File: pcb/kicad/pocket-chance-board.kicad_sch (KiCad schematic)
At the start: 144 parts, among them J1 SWD, J2 USB4085-GF-A, J3 LiPo JST-PH 2.0mm (1 = + RED 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, J4 LCD 1.54in ST7789 module, JST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, J5 Speaker JST-PH, J6 microSD Molex 104031-0811, J7 STEMMA QT, J8 Expansion (6 = VBAT_SENSE ADC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, J9 LCD header 2.54 mm (wire by n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, Q1 FS8205A, Q3 AO3400A, Q4 AO3401A, Q6 AO3401A (DNP: fit only for a 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, SW1 BOOT, SW10 DPAD LEFT PTS645SM43SMTR92, SW11 DPAD RIGHT PTS645SM43SMTR92, SW12 DPAD PRESS PTS645SM43SMTR92, SW2 RESET, SW3 POWER PCM12, SW4 A PTS125SM43SMTR2LFS, SW5 B PTS125SM43SMTR2LFS, SW6 X PTS125SM43SMTR2LFS, SW7 Y PTS125SM43SMTR2LFS, SW8 DPAD UP PTS645SM43SMTR92, SW9 DPAD DOWN PTS645SM43SMTR92, U1 RP2350A, U10 LSM6DSOXTR, U11 RM2, U2 W25Q128JVSIQ, U3 APS6404L-3SQR-SN, U4 USBLC6-2SC6, U5 BQ24074RGTR, U6 TPS63001DRCR, U7 DW01A, U8 PAM8302AADCR, U9 DS3231MZ+, Y1 12MHz ABM8-272-T3

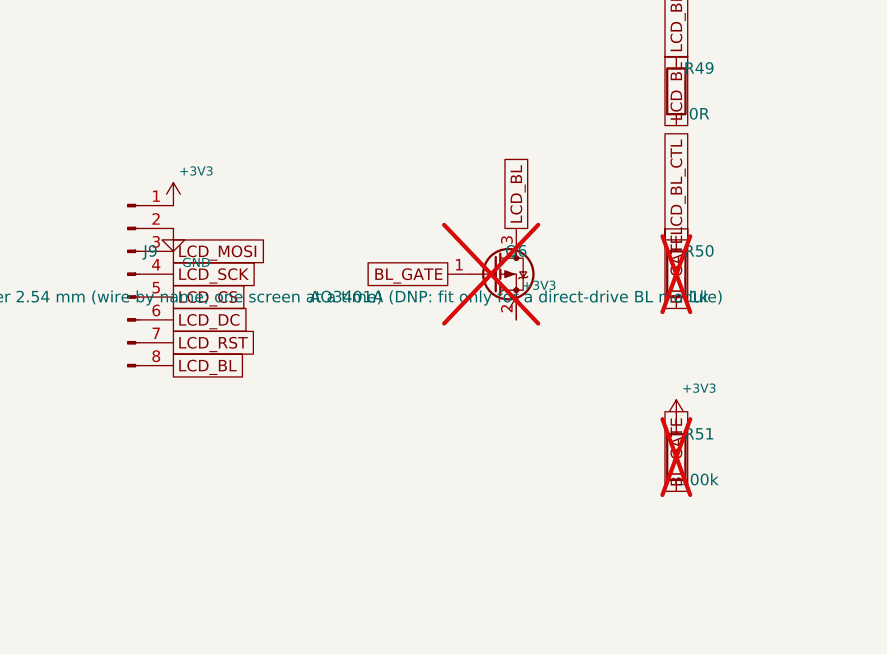
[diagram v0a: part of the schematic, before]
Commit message: Rev 0.12 (John's yes): R51 2.7k / R50 100R for the unfitted backlight switch, J9 in the AITRIP pin order, stronger R49 silk
Netlist diff vs rev 0.11 (5aee6a5): R50 1k -> 100R, R51 100k -> 2.7k, J9 pins remapped (GND, 3V3, SCK,
MOSI, RST, DC, CS, BL); nothing added or removed. ERC 0 errors, 2 expected warnings. Board regenerated
with stage-1 routing; DRC only unrouted connections.
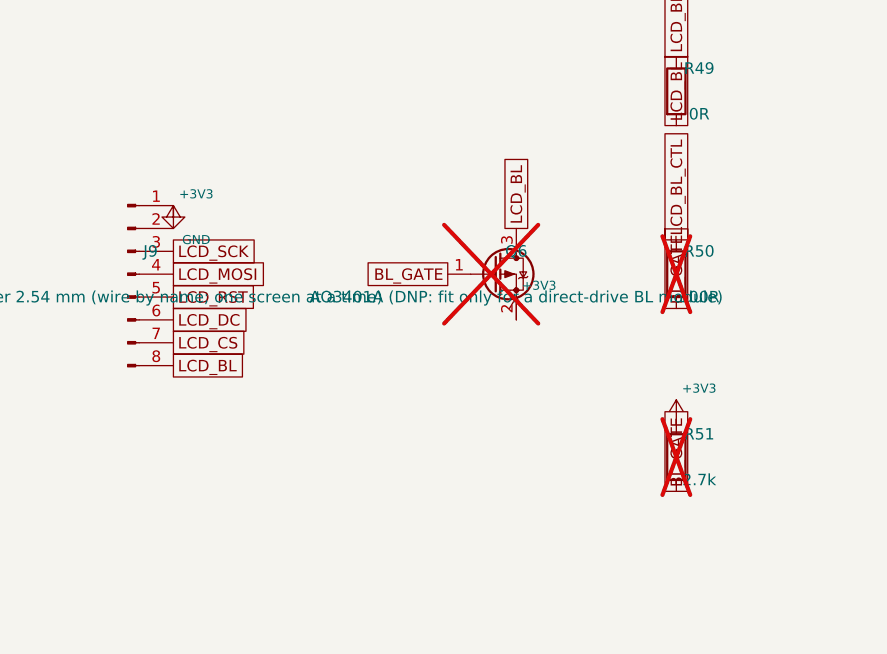
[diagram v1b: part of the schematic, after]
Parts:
- R50: value 1k -> 100R
- R51: value 100k -> 2.7k
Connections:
- net +3V3: now also J9.2 (Pin_2); no longer J9.1 (Pin_1)
- net GND: now also J9.1 (Pin_1); no longer J9.2 (Pin_2)
- net LCD_CS: now also J9.7 (Pin_7); no longer J9.5 (Pin_5)
- net LCD_MOSI: now also J9.4 (Pin_4); no longer J9.3 (Pin_3)
- net LCD_RST: now also J9.5 (Pin_5); no longer J9.7 (Pin_7)
- net LCD_SCK: now also J9.3 (Pin_3); no longer J9.4 (Pin_4)
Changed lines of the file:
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@@
 		(title "Pocket Chance board, spin 1")
 		(date "2026-10-04")
-		(rev "0.11")
+		(rev "0.12")
 		(company "Pocket Chance")
 		(comment 1 "Generated by pcb/tools/gen_sch.py from the connection table. Label-based: every pin carries its net name.")
@@
 	)
 	(symbol
-		(lib_id "power:+3V3")
+		(lib_id "power:GND")
 		(at 524.51 72.39 0)
 		(unit 1)
@@
 			)
 		)
-		(property "Value" "+3V3"
-			(at 527.05 68.58 0)
+		(property "Value" "GND"
+			(at 527.05 76.2 0)
 			(effects
 				(font
@@
 	)
 	(symbol
-		(lib_id "power:GND")
+		(lib_id "power:+3V3")
 		(at 524.51 74.93 0)
 		(unit 1)
@@
 			)
 		)
-		(property "Value" "GND"
-			(at 527.05 78.74 0)
+		(property "Value" "+3V3"
+			(at 527.05 71.12 0)
 			(effects
 				(font
@@
 		)
 	)
-	(global_label "LCD_MOSI"
+	(global_label "LCD_SCK"
 		(shape passive)
 		(at 524.51 77.47 0)
@@
 		)
 	)
-	(global_label "LCD_SCK"
+	(global_label "LCD_MOSI"
 		(shape passive)
 		(at 524.51 80.01 0)
@@
 		)
 	)
-	(global_label "LCD_CS"
+	(global_label "LCD_RST"
 		(shape passive)
 		(at 524.51 82.55 0)
@@
 		)
 	)
-	(global_label "LCD_RST"
+	(global_label "LCD_CS"
 		(shape passive)
 		(at 524.51 87.63 0)
@@
 			)
 		)
-		(property "Value" "1k"
+		(property "Value" "100R"
 			(at 582.93 82.55 0)
 			(effects
@@
 			)
 		)
-		(property "Value" "100k"
+		(property "Value" "2.7k"
 			(at 582.93 102.87 0)
 			(effects
